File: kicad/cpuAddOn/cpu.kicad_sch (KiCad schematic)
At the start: 56 parts, among them J5 TE_2311765-1, J7 Conn_02x13_Odd_Even, SW2 B3U-1000P[], U11 MX25R3235FM2IL0, U13 ICM-42605, U14 SHT40-AD1B-R2, U15 TCS34003FNM, U16 HDSP-7403, U6 STM32H743ZITx, U7 AS4C4M16SA-6TAN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

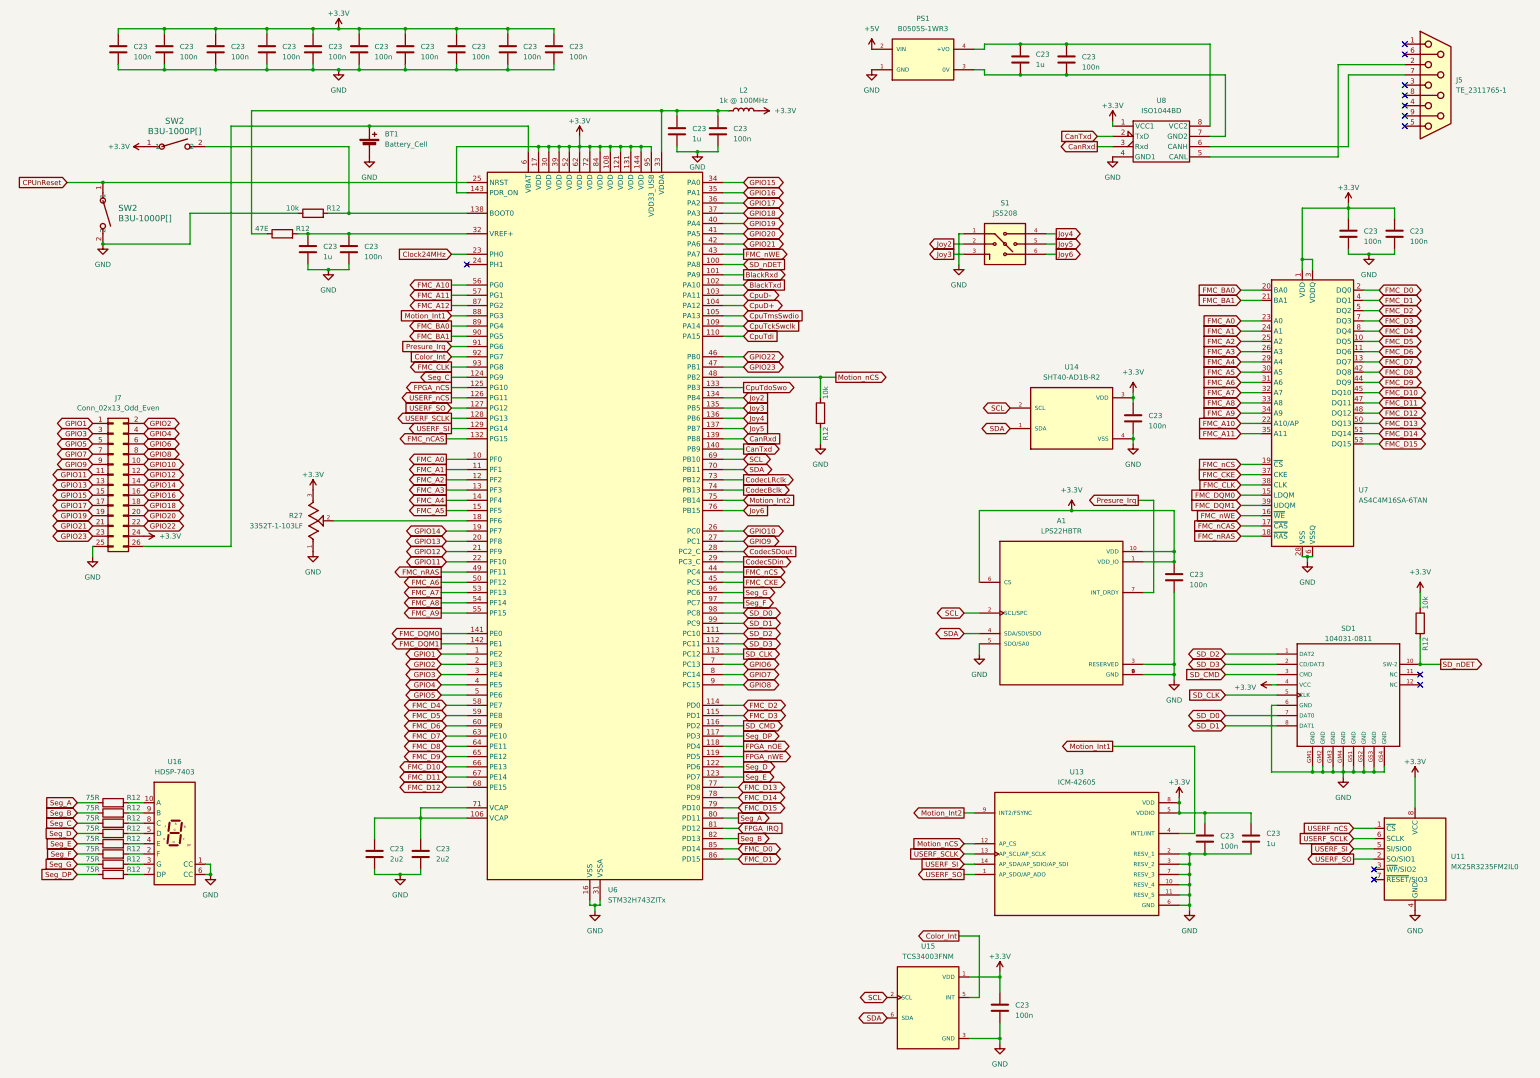
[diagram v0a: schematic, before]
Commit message: fixed bug with RS232 Added support for bigger SDRAMs Changed 7-segment display to SMD and active low
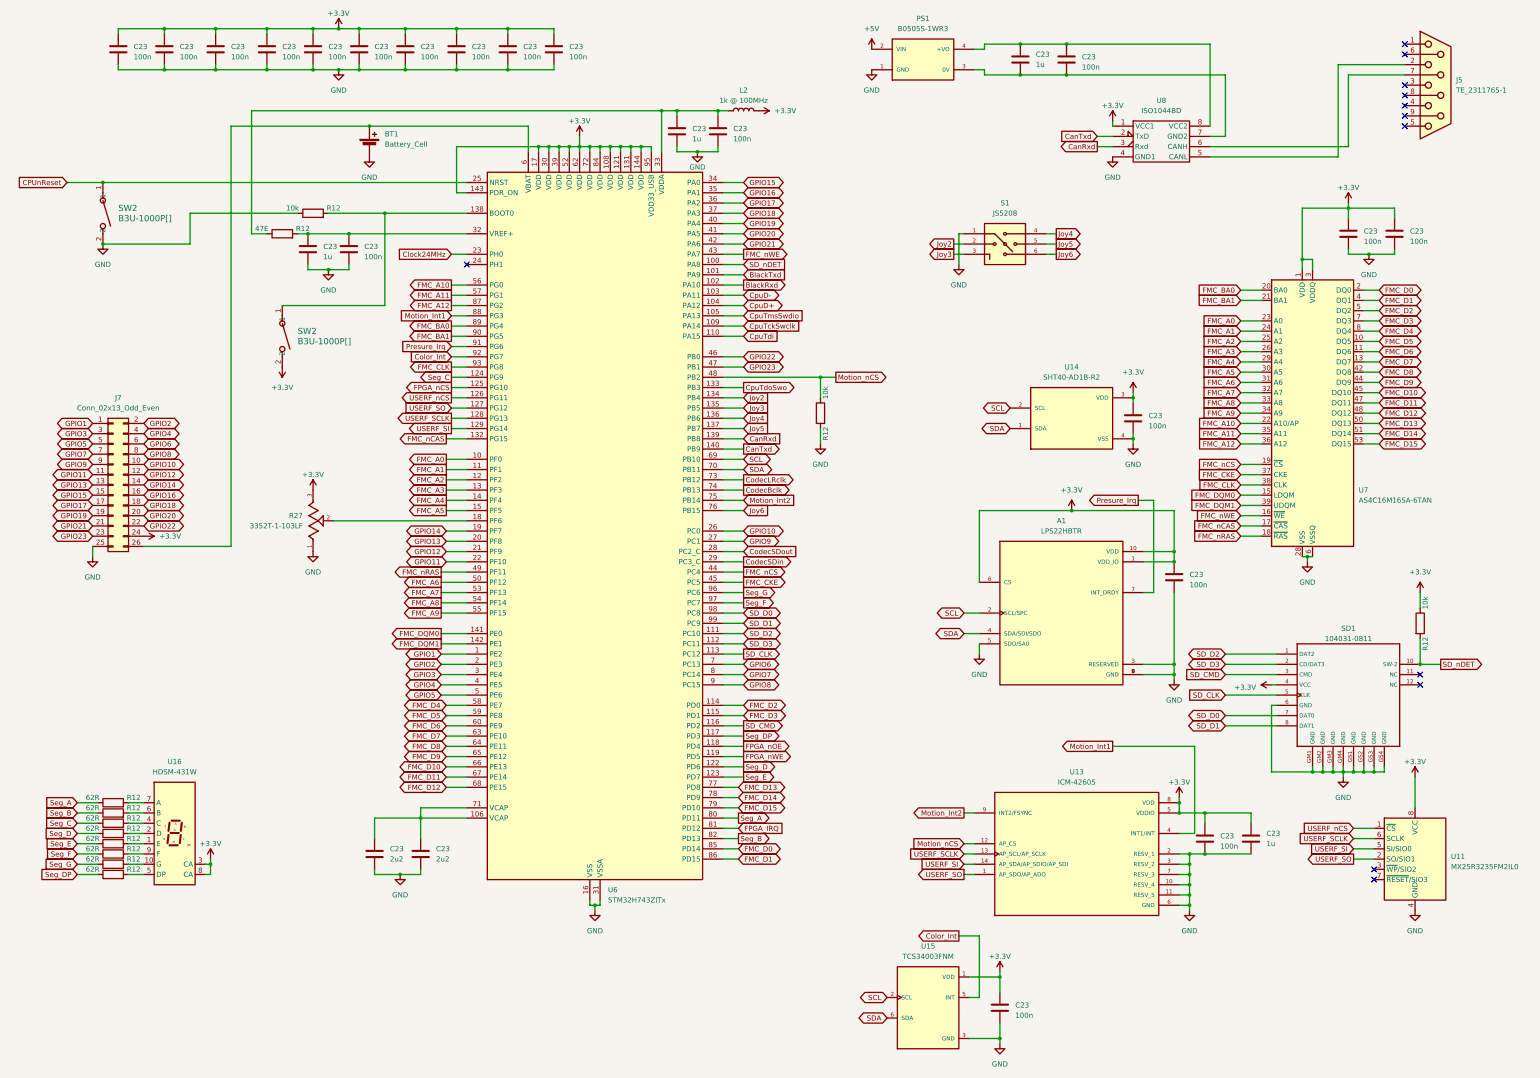
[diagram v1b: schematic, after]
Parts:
- R12: value 75R -> 62R
- U16: value HDSP-7403 -> HDSM-431W; footprint Display_7Segment:HDSP-7401 -> cpuAddOn:HDSM-431W
- U7: value AS4C4M16SA-6TAN -> AS4C16M16SA-6TAN
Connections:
- net +3.3V: now also SW2.2, U16.3 (CA), U16.8 (CA); no longer SW2.1
- net BlackRxd: now also U6.102 (PA10); no longer U6.101 (PA9)
- net BlackTxd: now also U6.101 (PA9); no longer U6.102 (PA10)
- net FMC_A12: now also U7.36 (NC)
- net GND: no longer U16.1 (CC), U16.6 (CC)
- net at R12.2: now also U16.2 (D); no longer U16.5 (D)
- net at R12.2: now also U16.4 (C); no longer U16.8 (C)
- net at R12.2, U6.138 (BOOT0): now also SW2.1; no longer SW2.2
- net at R12.2: now also U16.1 (E); no longer U16.4 (E)
- net at R12.2: now also U16.9 (F); no longer U16.2 (F)
- net at R12.2: now also U16.5 (DP); no longer U16.7 (DP)
- net at U16.10 (G): now also R12.2; no longer R12.2
- net at R12.2: now also U16.6 (B); no longer U16.9 (B)
- new net: R12.2, U16.7 (A)

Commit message: Made V1.1 of the cpu-addon
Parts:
- removed J7: Conn_02x13_Odd_Even, Connector_PinSocket_2.54mm:PinSocket_2x13_P2.54mm_Horizontal, symbol Connector_Generic:Conn_02x13_Odd_Even
- added C23 (x2): 9pF, Capacitor_SMD:C_0402_1005Metric, symbol Device:C
- added J7: Conn_02x16_Odd_Even, Connector_PinSocket_2.54mm:PinSocket_2x16_P2.54mm_Horizontal, symbol Connector_Generic:Conn_02x16_Odd_Even
- added Y1: RT2012-32.768-9-20-EXT-TR, Crystal:Crystal_SMD_2012-2Pin_2.0x1.2mm, symbol Device:Crystal
- BT1: footprint Battery:BatteryHolder_Keystone_2998_1x6.8mm -> Battery:BatteryHolder_Keystone_1060_1x2032
- U16: value HDSM-431W -> HDSM-433C
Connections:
- net GPIO1 is gone; now on net Joy3: U6.1 (PE2)
- net GPIO2 is gone; now on net Joy4: U6.2 (PE3)
- net GPIO3 is gone; now on net Joy5: U6.3 (PE4)
- net +3.3V: now also J7.1 (Pin_1), J7.19 (Pin_19), J7.2 (Pin_2), J7.20 (Pin_20); no longer U16.3 (CA), U16.8 (CA)
- net GND: now also U16.3 (CC), U16.8 (CC), C23.2, C23.2, J7.18 (Pin_18), J7.21 (Pin_21), J7.22 (Pin_22), J7.3 (Pin_3), J7.31 (Pin_31), J7.4 (Pin_4)
- net Joy3: no longer U6.135 (PB5)
- net Joy4: no longer U6.136 (PB6)
- net Joy5: no longer U6.137 (PB7)
- net at BT1.1 (+), U6.6 (VBAT): now also J7.32 (Pin_32)
- net GPIO10 renamed PMOD2_9
- net PMOD2_9: now also J7.26 (Pin_26)
- net GPIO11 renamed PMOD2_10
- net PMOD2_10: now also J7.24 (Pin_24)
- net GPIO12 renamed ADC_PWM3
- net ADC_PWM3: now also J7.15 (Pin_15)
- net GPIO13 renamed ADC_PWM2
- net ADC_PWM2: now also J7.16 (Pin_16)
- net GPIO14 renamed ADC4
- net ADC4: now also J7.17 (Pin_17)
- net GPIO15 renamed PMOD2_1
- net PMOD2_1: now also J7.29 (Pin_29)
- net GPIO16 renamed PMOD2_4
- net PMOD2_4: now also J7.23 (Pin_23)
- net GPIO17 renamed PMOD2_2
- net PMOD2_2: now also J7.27 (Pin_27)
- net GPIO18 renamed PMOD2_3
- net PMOD2_3: now also J7.25 (Pin_25)
- net GPIO19 renamed PMOD1_1
- net PMOD1_1: now also J7.11 (Pin_11)
- net GPIO20 renamed PMOD1_4
- net PMOD1_4: now also J7.5 (Pin_5)
- net GPIO21 renamed PMOD1_3
- net PMOD1_3: now also J7.7 (Pin_7)
- net GPIO22 renamed ADC_PWM0
- net ADC_PWM0: now also J7.14 (Pin_14)
- net GPIO23 renamed ADC_PWM1
- net ADC_PWM1: now also J7.13 (Pin_13)
- net GPIO4 renamed PMOD1_7
- net PMOD1_7: now also J7.12 (Pin_12)
- net GPIO5 renamed PMOD1_8
- net PMOD1_8: now also J7.10 (Pin_10)
- net GPIO6 renamed PMOD2_7
- net PMOD2_7: now also J7.30 (Pin_30)
- net GPIO7: no longer names the net of U6.8 (PC14)
- net GPIO7: now also C23.1, Y1.2
- net GPIO8: no longer names the net of U6.9 (PC15)
- net GPIO8: now also C23.1, Y1.1
- net GPIO9 renamed PMOD2_8
- net PMOD2_8: now also J7.28 (Pin_28)
- new net PMOD1_10: J7.6 (Pin_6), U6.137 (PB7)
- new net PMOD1_2: J7.9 (Pin_9), U6.135 (PB5)
- new net PMOD1_9: J7.8 (Pin_8), U6.136 (PB6)
